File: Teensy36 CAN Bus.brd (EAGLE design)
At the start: 86.2 x 17.8 mm, 42 parts, among them J1 CONN_34PIN_VERT, J2 CONN_34PIN_VERT, J3 SOLDER_POINT, J4 SOLDER_POINT, J5 SOLDER_POINT, J6 SOLDER_POINT, J7 SOLDER_POINT, J8 SOLDER_POINT, U1 SN65HVD230DR, U2 SN65HVD230DR

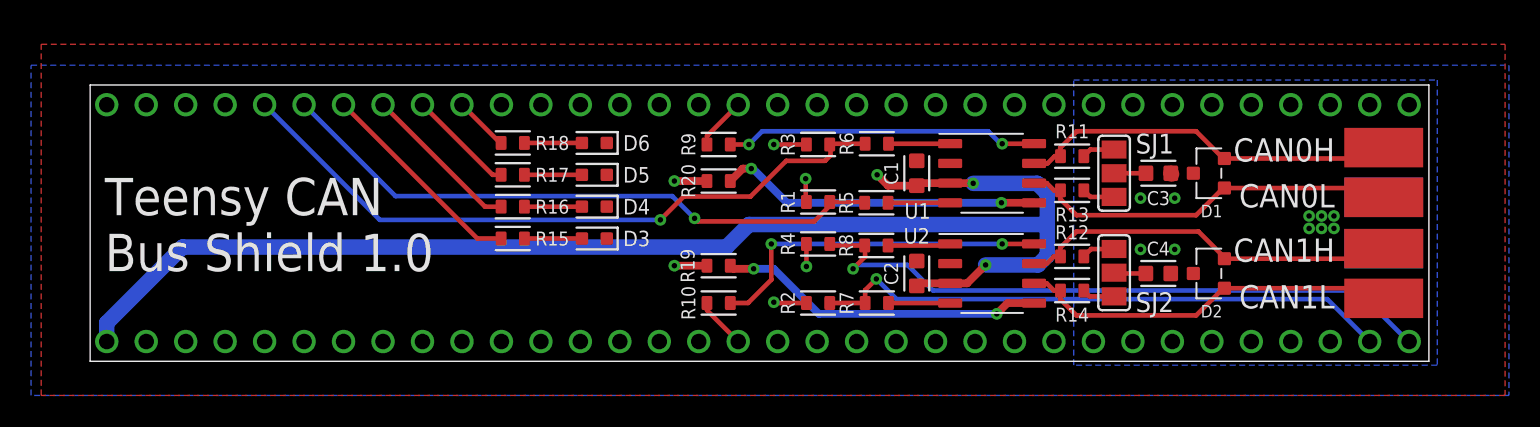
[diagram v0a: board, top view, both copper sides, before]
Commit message: Update Teensy pinout
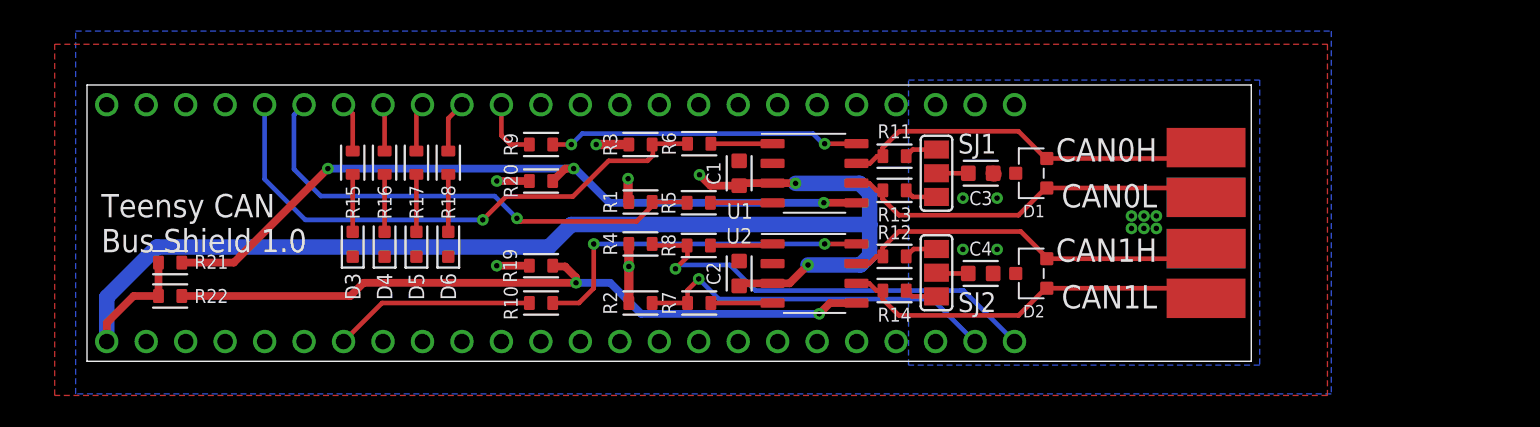
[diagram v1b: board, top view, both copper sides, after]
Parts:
- added R21, R22: 0Ω, AlphaLibrary:REST-0603
- J1, J2: value CONN_34PIN_VERT -> CONN_24PIN_VERT; device AlphaLibrary:CONN_100MIL_34_PIN -> AlphaLibrary:CONN_100MIL_24_PIN
- moved D3 15.6 mm to (17.1, 7.53), turned to 90 degrees
- moved D4 13.7 mm to (19.1, 7.53), turned to 90 degrees
- moved D5 12.3 mm to (21.2, 7.53), turned to 90 degrees
- moved D6 11.4 mm to (23.2, 7.53), turned to 90 degrees
- moved J3 11.4 mm to (72.0, 7.25)
- moved J4 11.4 mm to (72.0, 4.05)
- moved J5 11.4 mm to (72.0, 13.8)
- moved J6 11.4 mm to (72.0, 10.6)
- moved J7 11.4 mm to (72.0, 10.6)
- moved J8 11.4 mm to (72.0, 7.25)
- moved C1 11.4 mm to (42.0, 12.1)
- moved C2 11.4 mm to (42.0, 5.65)
- moved C3 11.4 mm to (57.5, 12.1)
- moved D1 11.4 mm to (60.8, 12.1)
- moved D2 11.4 mm to (60.8, 5.65)
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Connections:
- net 3V3: now also J2.15; no longer J2.25
- net 5V0: now also R21.2, R22.2
- net CAN1_RX: now also J1.23; no longer J1.33
- net CAN1_TX: now also J1.24; no longer J1.34
- net GND: now also J1.15; no longer J1.25
- net STBY0: now also J2.11; no longer J2.17
- net STBY1: now also J1.7; no longer J1.17
- net VIO0: now also R21.1
- net VIO1: now also R22.1
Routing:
- net VIO0: track 20.8 -> 48.5 mm, vias 2 -> 3
- net VIO1: track 21.1 -> 47.0 mm
- net CAN1_TX: track 42.1 -> 28.1 mm
- net CAN1_RX: track 37.5 -> 23.6 mm
- net D5: track 13.7 -> 3.22 mm
- net STBY1: track 3.31 -> 13.0 mm
- net CAN0_TX: track 44.3 -> 35.6 mm
- net CAN0_RX: track 39.9 -> 31.8 mm
- net D6: track 10.3 -> 3.02 mm
- net D7: track 6.93 -> 3.14 mm
- net 5V0: track 89.2 -> 86.1 mm
- net STBY0: track 3.39 -> 4.02 mm
- net 3V3: track 11.4 -> 11.6 mm, vias 6 -> 5
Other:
- board size 86.2 x 17.8 mm -> 74.9 x 17.8 mm
